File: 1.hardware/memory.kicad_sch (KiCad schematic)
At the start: 71 parts, among them IC2 IS42S32800J-6TLI, U3 W25Q128JVS, U4 NC_IS42S16400J-xC

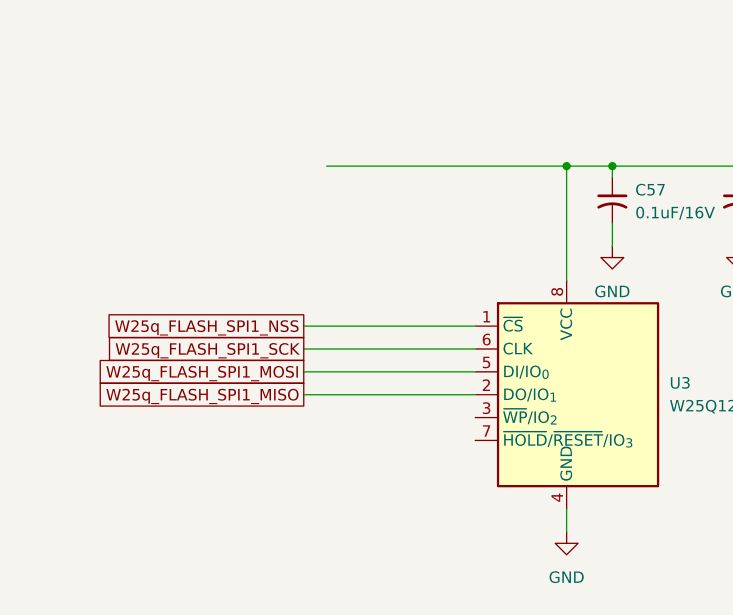
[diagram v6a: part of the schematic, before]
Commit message: 핀 배치 반영
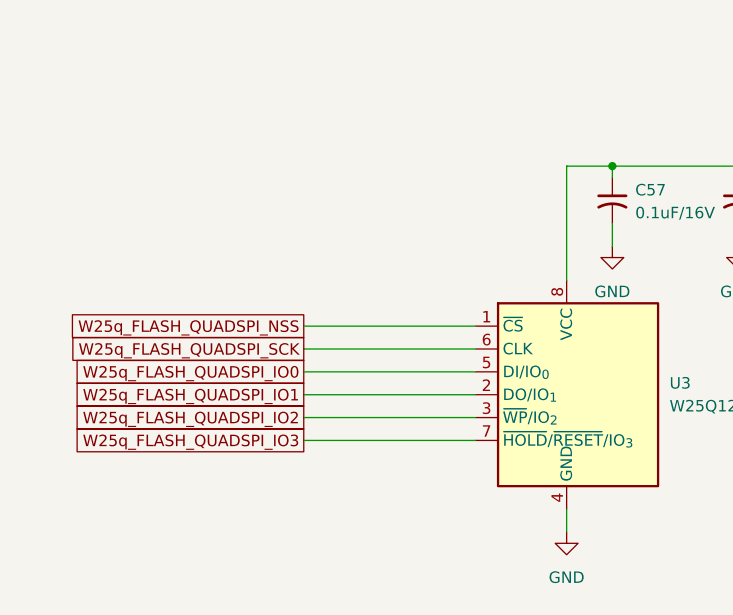
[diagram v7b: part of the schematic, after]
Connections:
- net W25q_FLASH_QUADSPI_IO2: now reaches U3.3 (~{WP}/IO_{2})
- net W25q_FLASH_QUADSPI_IO3: now reaches U3.7 (~{HOLD}/~{RESET}/IO_{3})
- net W25q_FLASH_SPI1_MISO renamed W25q_FLASH_QUADSPI_IO1
- net W25q_FLASH_SPI1_MOSI renamed W25q_FLASH_QUADSPI_IO0
- net W25q_FLASH_SPI1_NSS renamed W25q_FLASH_QUADSPI_NSS
- net W25q_FLASH_SPI1_SCK renamed W25q_FLASH_QUADSPI_SCK
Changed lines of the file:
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@@
 	)
 	(junction
-		(at 107.95 96.52)
-		(diameter 0)
-		(color 0 0 0 0)
-	)
-	(junction
 		(at 250.19 72.39)
 		(diameter 0)
@@
 	(wire
 		(pts
-			(xy 81.28 96.52) (xy 107.95 96.52)
-		)
-		(stroke
-			(width 0)
-			(type default)
-		)
-	)
-	(wire
-		(pts
 			(xy 350.52 123.19) (xy 355.6 123.19)
 		)
@@
 	(wire
 		(pts
+			(xy 78.74 127) (xy 97.79 127)
+		)
+		(stroke
+			(width 0)
+			(type default)
+		)
+	)
+	(wire
+		(pts
 			(xy 350.52 133.35) (xy 355.6 133.35)
 		)
@@
 	(wire
 		(pts
+			(xy 78.74 124.46) (xy 97.79 124.46)
+		)
+		(stroke
+			(width 0)
+			(type default)
+		)
+	)
+	(wire
+		(pts
 			(xy 350.52 163.83) (xy 355.6 163.83)
 		)
@@
 		)
 	)
-	(global_label "W25q_FLASH_SPI1_MISO"
+	(global_label "W25q_FLASH_QUADSPI_IO1"
 		(shape passive)
 		(at 78.74 121.92 180)
@@
 		)
 		(property "Intersheetrefs" "${INTERSHEET_REFS}"
-			(at 54.3086 121.92 0)
+			(at 51.9499 121.92 0)
 			(effects
 				(font
@@
 		)
 	)
+	(global_label "W25q_FLASH_QUADSPI_IO2"
+		(shape passive)
+		(at 78.74 124.46 180)
+		(fields_autoplaced yes)
+		(effects
+			(font
+				(size 1.27 1.27)
+			)
+			(justify right)
+		)
+		(property "Intersheetrefs" "${INTERSHEET_REFS}"
+			(at 51.9499 124.46 0)
+			(effects
+				(font
+					(size 1.27 1.27)
+				)
+				(justify right)
+				(hide yes)
+			)
+		)
+	)
 	(global_label "SDRAM_VDDQ"
 		(shape passive)
@@
 		)
 	)
-	(global_label "W25q_FLASH_SPI1_MOSI"
+	(global_label "W25q_FLASH_QUADSPI_IO0"
 		(shape passive)
 		(at 78.74 119.38 180)
@@
 		)
 		(property "Intersheetrefs" "${INTERSHEET_REFS}"
-			(at 54.3086 119.38 0)
+			(at 51.9499 119.38 0)
 			(effects
 				(font
@@
 		)
 	)
-	(global_label "W25q_FLASH_SPI1_NSS"
+	(global_label "W25q_FLASH_QUADSPI_NSS"
 		(shape passive)
 		(at 78.74 114.3 180)
@@
 		)
 		(property "Intersheetrefs" "${INTERSHEET_REFS}"
-			(at 55.1553 114.3 0)
+			(at 51.3452 114.3 0)
 			(effects
 				(font
@@
 		)
 	)
+	(global_label "W25q_FLASH_QUADSPI_IO3"
+		(shape passive)
+		(at 78.74 127 180)
+		(fields_autoplaced yes)
+		(effects
+			(font
+				(size 1.27 1.27)
+			)
+			(justify right)
+		)
+		(property "Intersheetrefs" "${INTERSHEET_REFS}"
+			(at 51.9499 127 0)
+			(effects
+				(font
+					(size 1.27 1.27)
+				)
+				(justify right)
+				(hide yes)
+			)
+		)
+	)
 	(global_label "SDRAM_VDD"
 		(shape passive)
@@
 		)
 	)
-	(global_label "W25q_FLASH_SPI1_SCK"
+	(global_label "W25q_FLASH_QUADSPI_SCK"
 		(shape passive)
 		(at 78.74 116.84 180)
@@
 		)
 		(property "Intersheetrefs" "${INTERSHEET_REFS}"
-			(at 55.1553 116.84 0)
+			(at 51.3452 116.84 0)
 			(effects
 				(font

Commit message: 중간 저장
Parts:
- C62: renamed from C57; value 0.1uF/16V -> 0.1uF/50V; footprint Capacitor_SMD:C_0402_1005Metric -> Capacitor_SMD:C_0603_1608Metric
- C63: renamed from C41; value 0.1uF/16V -> 0.1uF/50V; footprint Capacitor_SMD:C_0402_1005Metric -> Capacitor_SMD:C_0603_1608Metric
- C64: renamed from C58; value 0.1uF/16V -> 0.1uF/50V; footprint Capacitor_SMD:C_0402_1005Metric -> Capacitor_SMD:C_0603_1608Metric
- C66: renamed from C42; value 0.1uF/16V -> 0.1uF/50V; footprint Capacitor_SMD:C_0402_1005Metric -> Capacitor_SMD:C_0603_1608Metric
- C67: renamed from C43; value 0.1uF/16V -> 0.1uF/50V; footprint Capacitor_SMD:C_0402_1005Metric -> Capacitor_SMD:C_0603_1608Metric
- C68: renamed from C44; value 0.1uF/16V -> 0.1uF/50V; footprint Capacitor_SMD:C_0402_1005Metric -> Capacitor_SMD:C_0603_1608Metric
- C69: renamed from C45; value 0.1uF/16V -> 0.1uF/50V; footprint Capacitor_SMD:C_0402_1005Metric -> Capacitor_SMD:C_0603_1608Metric
- C70: renamed from C46; value 0.1uF/16V -> 0.1uF/50V; footprint Capacitor_SMD:C_0402_1005Metric -> Capacitor_SMD:C_0603_1608Metric
- C71: renamed from C47; value 0.1uF/16V -> 0.1uF/50V; footprint Capacitor_SMD:C_0402_1005Metric -> Capacitor_SMD:C_0603_1608Metric
- C73: renamed from C49; value 0.1uF/16V -> 0.1uF/50V; footprint Capacitor_SMD:C_0402_1005Metric -> Capacitor_SMD:C_0603_1608Metric
- renumbered C59 to C65, C48 to C72, IC2 to IC3, R84 to R100, R85 to R101, R86 to R102, R87 to R103, R88 to R104, R89 to R105, R34 to R50, R35 to R51, R36 to R52, R37 to R53, R38 to R54, R39 to R55, R40 to R56, R41 to R57, R42 to R58, R43 to R59, R44 to R60, R45 to R61, R46 to R62, R47 to R63, R48 to R64, R49 to R65, R50 to R66, R51 to R67, R52 to R68, R53 to R69, R54 to R70, R55 to R71, R56 to R72, R57 to R73, R58 to R74, R59 to R75, R60 to R76, R61 to R77, R62 to R78, R63 to R79, R64 to R80, R65 to R81, R66 to R82, R67 to R83, R68 to R84, R69 to R85, R70 to R86, R71 to R87, R72 to R88, R73 to R89, R74 to R90, R75 to R91, R76 to R92, R77 to R93, R78 to R94, R79 to R95, R80 to R96, R81 to R97, R82 to R98, R83 to R99, U3 to U5, U4 to U6
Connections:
- net 3V3_MCU: now also IC3.43 (VDD_4)
- no-connect marks 6 -> 8
